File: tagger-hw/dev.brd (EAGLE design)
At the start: 100 x 80 mm, 7 parts, among them IC1 4050D, IC2 LP298XS, X1 MICROSD

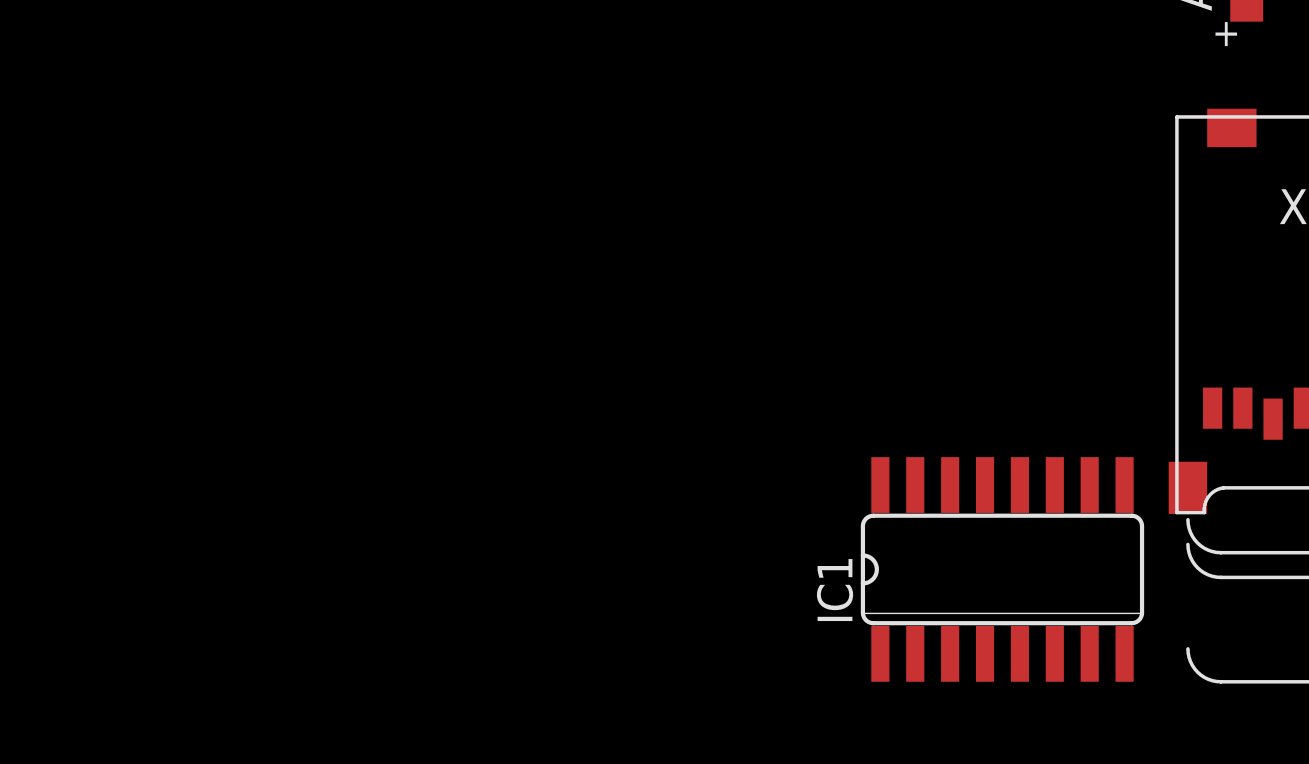
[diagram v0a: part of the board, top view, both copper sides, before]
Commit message: Add Arduino example, rename main to dev
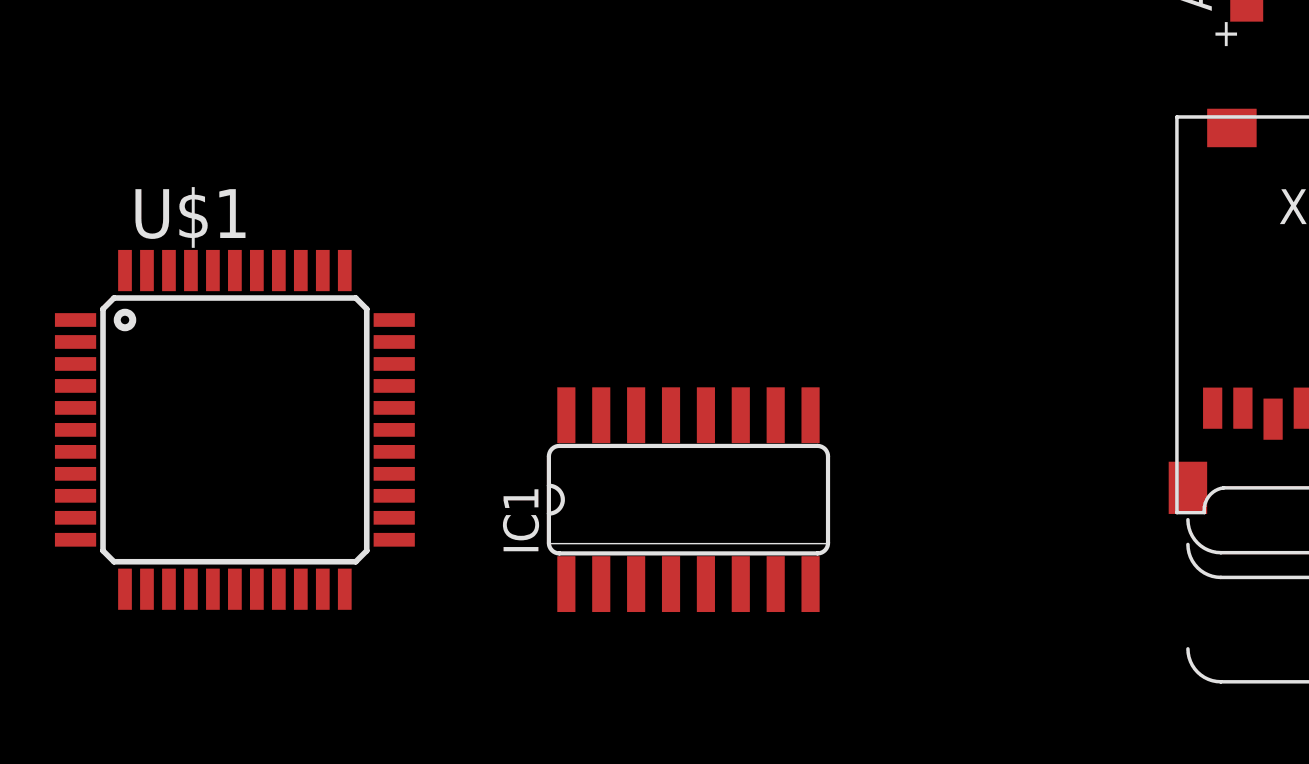
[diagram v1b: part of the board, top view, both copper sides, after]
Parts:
- added U$1: ATMEGA32U4-AU, adafruit:TQFP44
- IC1: value 4050D -> 4010D
- moved IC1 11.7 mm to (-45.7, 7.62)
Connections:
- net DO renamed MISO
- removed net CLK: IC1.3, IC1.9
- removed net DI: IC1.5
- new net MOSI: IC1.3
- new net SCK: IC1.5, IC1.9
- net +3V3: now also IC1.16
- net N$2: now also IC1.4; no longer IC1.2
- net N$5: now also IC1.2; no longer IC1.4
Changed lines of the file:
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@@
 </variantdefs>
 <classes>
-<class number="0" name="default" width="0" drill="0">
+<class number="0" name="default" width="0.254" drill="0.6096">
+<clearance class="0" value="0.254"/>
+</class>
+<class number="1" name="power" width="0.254" drill="0.6096">
+<clearance class="1" value="0.254"/>
+</class>
+<class number="2" name="gnd" width="0.254" drill="0.6096">
+<clearance class="2" value="0.254"/>
+</class>
+<class number="3" name="usbvcc" width="0.254" drill="0.6096">
+<clearance class="3" value="0.254"/>
+</class>
+<class number="4" name="aref" width="0.254" drill="0.6096">
+<clearance class="4" value="0.254"/>
 </class>
 </classes>
@@
 <element name="C1" library="adafruit" package="A/3216-18R" value="10uF/10V" x="-35.56" y="26.67"/>
 <element name="C2" library="adafruit" package="C0805K" value="0.1uF" x="-16.51" y="40.64"/>
-<element name="IC1" library="40xx" package="SO16" value="4050D" x="-34.29" y="5.08"/>
 <element name="IC2" library="adafruit" package="SOT23-5L" value="LP298XS" x="-19.05" y="26.67"/>
 <element name="R1" library="adafruit" package="R0805" value="1K" x="-15.24" y="34.29"/>
 <element name="X1" library="adafruit" package="MICROSD" value="MICROSD" x="-27.94" y="21.59"/>
+<element name="IC1" library="40xx" library_urn="urn:adsk.eagle:library:80" package="SO16" package3d_urn="urn:adsk.eagle:package:821/2" value="4010D" x="-45.72" y="7.62"/>
+<element name="U$1" library="adafruit" package="TQFP44" value="ATMEGA32U4-AU" x="-62.23" y="10.16"/>
 </elements>
 <signals>
@@
 <contactref element="ACT" pad="A"/>
 <contactref element="IC1" pad="10"/>
-<wire x1="-25.4" y1="25.62" x2="-31.115" y2="8.1534" width="0" layer="19" extent="1-1"/>
+<wire x1="-25.4" y1="25.62" x2="-42.545" y2="10.6934" width="0" layer="19" extent="1-1"/>
 </signal>
 <signal name="N$2">
-<contactref element="IC1" pad="2"/>
 <contactref element="X1" pad="5"/>
-<wire x1="-23.34" y1="10.95" x2="-37.465" y2="2.0066" width="0" layer="19" extent="1-1"/>
+<contactref element="IC1" pad="4"/>
+<wire x1="-23.34" y1="10.95" x2="-46.355" y2="4.5466" width="0" layer="19" extent="1-1"/>
 </signal>
 <signal name="N$3">
-<contactref element="IC1" pad="6"/>
 <contactref element="X1" pad="2"/>
 <contactref element="R1" pad="1"/>
-<wire x1="-20.04" y1="11.35" x2="-32.385" y2="2.0066" width="0" layer="19" extent="1-1"/>
+<contactref element="IC1" pad="6"/>
+<wire x1="-20.04" y1="11.35" x2="-43.815" y2="4.5466" width="0" layer="19" extent="1-1"/>
 <wire x1="-16.24" y1="34.29" x2="-20.04" y2="11.35" width="0" layer="19" extent="1-1"/>
 </signal>
 <signal name="+3V3">
 <contactref element="X1" pad="4"/>
-<contactref element="IC1" pad="1"/>
 <contactref element="IC2" pad="5"/>
 <contactref element="C1" pad="+"/>
-<wire x1="-22.24" y1="10.55" x2="-38.735" y2="2.0066" width="0" layer="19" extent="1-1"/>
-<wire x1="-20" y1="27.97" x2="-22.24" y2="10.55" width="0" layer="19" extent="1-1"/>
-<wire x1="-34.185" y1="26.67" x2="-20" y2="27.97" width="0" layer="19" extent="1-1"/>
+<contactref element="IC1" pad="16"/>
+<contactref element="IC1" pad="1"/>
+<wire x1="-50.165" y1="10.6934" x2="-50.165" y2="4.5466" width="0" layer="19" extent="1-1"/>
+<wire x1="-34.185" y1="26.67" x2="-50.165" y2="10.6934" width="0" layer="19" extent="1-1"/>
+<wire x1="-20" y1="27.97" x2="-34.185" y2="26.67" width="0" layer="19" extent="1-1"/>
+<wire x1="-22.24" y1="10.55" x2="-20" y2="27.97" width="0" layer="19" extent="1-1"/>
 </signal>
 <signal name="GND">
@@
 <contactref element="X1" pad="MT2"/>
 <contactref element="X1" pad="MT1"/>
-<contactref element="IC1" pad="8"/>
 <contactref element="IC2" pad="2"/>
 <contactref element="C1" pad="-"/>
 <contactref element="C2" pad="2"/>
+<contactref element="IC1" pad="8"/>
+<contactref element="IC1" pad="14"/>
 <contactref element="IC1" pad="11"/>
-<contactref element="IC1" pad="14"/>
-<wire x1="-27.54" y1="8.05" x2="-29.845" y2="2.0066" width="0" layer="19" extent="1-1"/>
+<wire x1="-43.815" y1="10.6934" x2="-41.275" y2="4.5466" width="0" layer="19" extent="1-1"/>
+<wire x1="-47.625" y1="10.6934" x2="-43.815" y2="10.6934" width="0" layer="19" extent="1-1"/>
+<wire x1="-27.54" y1="8.05" x2="-41.275" y2="4.5466" width="0" layer="19" extent="1-1"/>
 <wire x1="-24.44" y1="10.55" x2="-27.54" y2="8.05" width="0" layer="19" extent="1-1"/>
-<wire x1="-32.385" y1="8.1534" x2="-27.54" y2="8.05" width="0" layer="19" extent="1-1"/>
-<wire x1="-36.195" y1="8.1534" x2="-32.385" y2="8.1534" width="0" layer="19" extent="1-1"/>
 <wire x1="-14.34" y1="7.15" x2="-24.44" y2="10.55" width="0" layer="19" extent="1-1"/>
 <wire x1="-19.05" y1="25.37" x2="-24.44" y2="10.55" width="0" layer="19" extent="1-1"/>
 <wire x1="-15.51" y1="40.64" x2="-19.05" y2="25.37" width="0" layer="19" extent="1-1"/>
-<wire x1="-36.935" y1="26.67" x2="-19.05" y2="25.37" width="0" layer="19" extent="1-1"/>
+<wire x1="-36.935" y1="26.67" x2="-43.815" y2="10.6934" width="0" layer="19" extent="1-1"/>
 </signal>
 <signal name="VCC">
@@
 <contactref element="X1" pad="CD1"/>
 </signal>
-<signal name="DO">
+<signal name="MISO">
 <contactref element="X1" pad="7"/>
-</signal>
-<signal name="DI">
-<contactref element="IC1" pad="5"/>
-</signal>
-<signal name="CLK">
-<contactref element="IC1" pad="3"/>
-<contactref element="IC1" pad="9"/>
-<wire x1="-29.845" y1="8.1534" x2="-36.195" y2="2.0066" width="0" layer="19" extent="1-1"/>
-</signal>
-<signal name="CS">
-<contactref element="IC1" pad="7"/>
 </signal>
 <signal name="N$4">
@@
 <signal name="N$5">
 <contactref element="X1" pad="3"/>
-<contactref element="IC1" pad="4"/>
-<wire x1="-21.14" y1="10.95" x2="-34.925" y2="2.0066" width="0" layer="19" extent="1-1"/>
+<contactref element="IC1" pad="2"/>
+<wire x1="-21.14" y1="10.95" x2="-48.895" y2="4.5466" width="0" layer="19" extent="1-1"/>
+</signal>
+<signal name="MOSI">
+<contactref element="IC1" pad="3"/>
+</signal>
+<signal name="SCK">
+<contactref element="IC1" pad="5"/>
+<contactref element="IC1" pad="9"/>
+<wire x1="-41.275" y1="10.6934" x2="-45.085" y2="4.5466" width="0" layer="19" extent="1-1"/>
+</signal>
+<signal name="CS">
+<contactref element="IC1" pad="7"/>
 </signal>
 </signals>
 </board>
 </drawing>
+<compatibility>
+<note version="8.2" severity="warning">
+Since Version 8.2, EAGLE supports online libraries. The ids
+of those online libraries will not be understood (or retained)
+with this version.
+</note>
+<note version="8.3" severity="warning">
+Since Version 8.3, EAGLE supports URNs for individual library
+assets (packages, symbols, and devices). The URNs of those assets
+will not be understood (or retained) with this version.
+</note>
+<note version="8.3" severity="warning">
+Since Version 8.3, EAGLE supports the association of 3D packages
+with devices in libraries, schematics, and board files. Those 3D
+packages will not be understood (or retained) with this version.
+</note>
+</compatibility>
 </eagle>

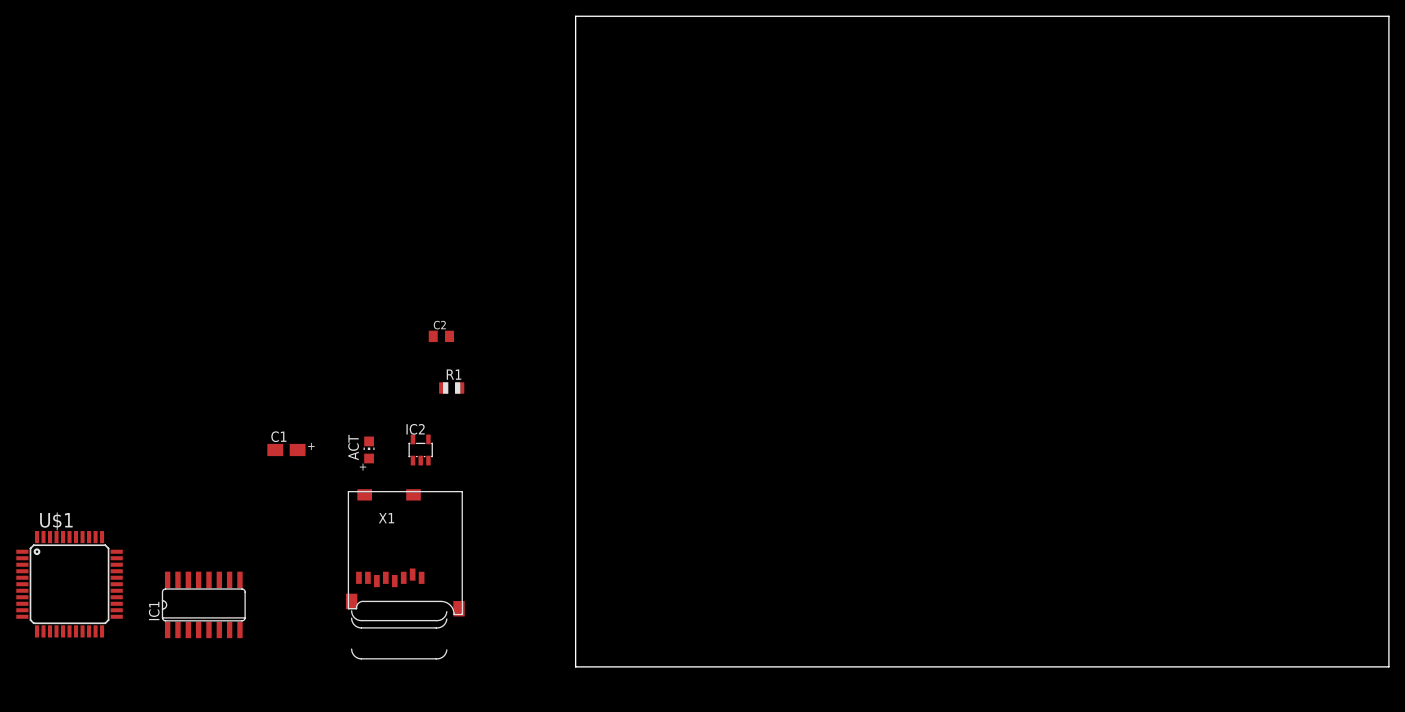
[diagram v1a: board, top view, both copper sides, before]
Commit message: Placement/layout done except for SPI RTC
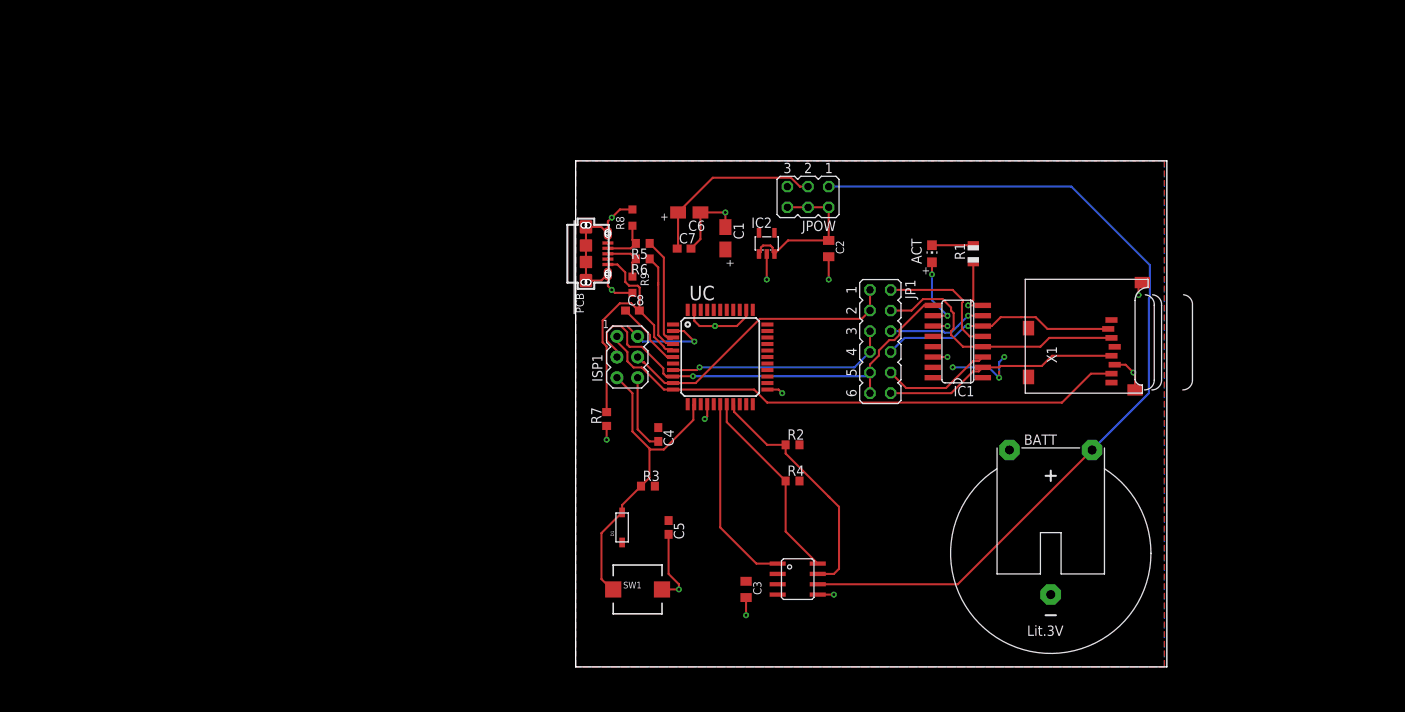
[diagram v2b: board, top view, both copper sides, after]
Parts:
- removed U$1: ATMEGA32U4-AU, adafruit:TQFP44
- added BATT: CR2430H, battery:CR2430H
- added C3: 0.1uF, adafruit:C0805K
- added C4, C8: 1uF, rcl:C0603
- added C5, C7: 100n, rcl:C0603
- added C6: 10uF/10V, adafruit:A/3216-18R
- added D1: (no value), adafruit:SOD-123
- added ISP1: AVRISP-6, adafruit:AVRISP
- added J1: SMARTPRJ_MYCON2_USB-MINI-B, dorskyee:SMARTPRJ_CON2_USB_MICRO_B_AT
- added JP1: (no value), jumper:JP6Q
- added JPOW: (no value), jumper:JP3Q
- added R2, R4: 4.7k, resistor:R0603
- added R3: 10k, resistor:R0603
- added R5, R6: 22, resistor:R0603
- added R7: 0, resistor:R0603
- added R8, R9: VARISTORCN0603, varistor:CT/CN0603
- added SW1: (no value), adafruit:PUSHBUTTON_SMD_SJ
- added UC: ATMEGA32U4-AU, adafruit:TQFP44
- added UCLK: DS3231MDS3231MZ+, dorskyee:S8MK+1
- moved IC1 98.2 mm to (47.0, 40.0), turned to 90 degrees
- moved X1 84.1 mm to (55.2, 33.7), turned to 90 degrees
- moved ACT 73.3 mm to (43.8, 50.8)
- moved R1 66.2 mm to (48.9, 50.8), turned to 90 degrees
- moved C1 59.9 mm to (18.4, 52.7), turned to 270 degrees
- moved IC2 49.6 mm to (23.5, 52.1)
- moved C2 48.8 mm to (31.1, 51.4), turned to 270 degrees
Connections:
- net N$1 renamed SD_ACT
- net N$4 renamed SD_ACT_D
- removed net CD: X1.CD1
- removed net CS: IC1.7
- removed net N$2: IC1.4, X1.5
- removed net N$3: IC1.6, R1.1, X1.2
- removed net N$5: IC1.2, X1.3
- new net CS_BUF: IC1.7, JP1.6
- new net CS_OUT: IC1.6, JP1.8, X1.2
- new net CS_SD: JP1.5, JP1.7, UC.8
- new net D+: J1.P3, R6.2, R9.1
- new net D+_R: R6.1, UC.4
- new net D-: J1.P2, R5.2, R8.1
- new net D-_R: R5.1, UC.3
- new net EXT_CLK: UC.17, UCLK.P$1
- new net MOSI_BUF: IC1.5, JP1.2
- new net MOSI_OUT: IC1.4, JP1.4, X1.3
- new net RESET: D1.A, ISP1.5, R3.1, SW1.P$2, UC.13
- new net SCK_BUF: IC1.3, JP1.10
- new net SCK_OUT: IC1.2, JP1.12, X1.5
- new net SCL: R4.1, UC.18, UCLK.P$8
- new net SDA: R2.1, UC.19, UCLK.P$7
- new net UCAP: C8.1, UC.6
- new net UGND: C8.2, J1.P5, R7.2, UC.5
- new net VBAT: BATT.+, JPOW.1, UCLK.P$6
- new net VBUS: C6.+, C7.1, JPOW.3
- new net VBUS_L: J1.P1
- new net VEXT: JPOW.5
- net +3V3: now also C3.1, C4.1, C5.1, D1.C, ISP1.2, R2.2, R3.2, R4.2, UC.14, UC.2, UC.24, UC.34, UC.44, UCLK.P$2
- net GND: now also BATT.-, C3.2, C4.2, C5.2, C6.-, C7.2, ISP1.6, J1.S1, J1.S2, J1.S3, J1.S4, J1.S5, J1.S6, R1.1, R7.1, R8.2, R9.2, SW1.P$1, UC.15, UC.23, UC.35, UC.43, UCLK.P$5
- net MISO: now also ISP1.1, UC.11
- net MOSI: now also ISP1.4, JP1.1, JP1.3, UC.10; no longer IC1.3
- net SCK: now also ISP1.3, JP1.11, JP1.9, UC.9; no longer IC1.5
- net VCC: now also JPOW.2, JPOW.4, JPOW.6
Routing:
- net VBAT: track 0.00 -> 109.7 mm
- net GND: track 0.00 -> 94.0 mm, vias 0 -> 17
- net MISO: track 0.00 -> 66.7 mm
- net SCK: track 0.00 -> 55.3 mm, vias 0 -> 1
- net RESET: track 0.00 -> 39.8 mm
- net MOSI: track 0.00 -> 36.1 mm
- net UGND: track 0.00 -> 33.2 mm
- net MOSI_OUT: track 0.00 -> 32.8 mm
- net SDA: track 0.00 -> 29.8 mm
- net CS_OUT: track 0.00 -> 29.1 mm, vias 0 -> 1
- net SCK_OUT: track 0.00 -> 29.1 mm
- net CS_SD: track 0.00 -> 27.7 mm, vias 0 -> 1
- net SCL: track 0.00 -> 24.2 mm
- net EXT_CLK: track 0.00 -> 24.1 mm
- net VBUS: track 0.00 -> 22.7 mm
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- added copper zone on layer 1, net +3V3
- added copper zone on layer 16, net GND
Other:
- board size 100 x 80 mm -> 72.7 x 62.2 mm
